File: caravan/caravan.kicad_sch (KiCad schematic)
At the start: 50 parts

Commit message: Updated caravan
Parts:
- added D?: Diode, Diode_THT:D_DO-41_SOD81_P10.16mm_Horizontal, symbol Diode:1N4007
- added K?: Relay_Automotive_SPDT, symbol microfarad-de:Relay_Automotive_SPDT
- CB?: value (none) -> FI-Schalter
- CB? (x2): value (none) -> LS-Schalter
- D?: value (none) -> Diode; footprint (none) -> Diode_THT:D_DO-41_SOD81_P10.16mm_Horizontal
- F? (x4): value (none) -> 10A
- F?: value (none) -> 100A MEGA
- F?: value (none) -> 2A
- F?: value (none) -> 1A
- F? (x3): value (none) -> 15A
- F? (x3): value (none) -> 5A
- F? (x2): value (none) -> 25A Maxi
- F? (x4): value (none) -> 30A MIDI
- K?: value (none) -> 40A
- P?: value (none) -> Landstrom
- Q?: value (none) -> BC337; footprint (none) -> Package_TO_SOT_THT:TO-92_Inline
- R: value (none) -> 100KΩ
- R?, SW? (x3): value (none) -> (none)
- SC?: value (none) -> Solarpanele
- SW?: value (none) -> Hauptschalter
- TH? (x3): value (none) -> Temp. Sensor
- U?: value (none) -> 12V-24V-Wandler
- U?: value (none) -> Victron SmartShunt 500A
- U?: value (none) -> Anhängerstecker
- U?: value (none) -> BMS 100A
- U? (x4): value (none) -> LiFePo4
- U?: value (none) -> Dometic 10 Kühlschrank
- U?: value (none) -> Victron SmartSolar
- U?: value (none) -> Votronic VCC 1212-20 C
- U?: value (none) -> AL-KO ATC
- U?: value (none) -> Ideale Diode 15A
- U?: value (none) -> Victron Blue Smart IP22
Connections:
- net Earth: now also D?.2 (A), F?.1, K?.86, D?.2 (A), K?.30, K?.86, K?.87a
- new net: CB?.1, U?.~ (PE), U?.~ (PE)
- new net: CB?.3, U?.~ (PE), U?.~ (PE)
- new net: D?.1 (K), K?.85, K?.87, U?.~ (PV-)
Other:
- note added: "Kühlschrank-Vorrangschaltung: Leitet überschüssige Solarenergie in den Absorber-Kühlschrank um."
- note added: "MPPT 100/20 Solarladeregler"
- note added: "SunPower 2x120 Watt"

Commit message: Updated caravan and water-sensor
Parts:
- removed D? (x2): Diode, Diode_THT:D_DO-41_SOD81_P10.16mm_Horizontal, symbol Diode:1N4007
- added D? (x2): 1N4007, Diode_THT:D_DO-41_SOD81_P10.16mm_Horizontal, symbol Diode:1N4007
- added F? (x3): 1A, symbol Device:Fuse
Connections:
- net 25mm2 is gone; now on net Earth: F?.1, F?.2, SW?.1 (A), TH?.1, U?.~ (-), U?.~ (-), U?.~ (TS), U?.~ (VBatt+)
- net Earth: now also F?.2, F?.2, F?.2, F?.2, F?.2, K?.85, K?.87, F?.2, F?.2; no longer SW?.2 (B)
- new net: CB?.1, U?.~ (PE), U?.~ (PE)
- new net: CB?.3, U?.~ (PE), U?.~ (PE)
- new net: D?.1 (K), D?.1 (K), U?.~ (PE)
- new net: F?.1, U?.~ (PV-)
- new net: F?.1, SW?.2 (B)
- new net: D?.2 (A), F?.1
- new net: D?.2 (A), F?.2
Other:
- note added: "12V- Verteiler unten"
- note added: "12V-Verteiler oben"
- note added: "4x Wago-Klemmen"
- note added: "ATC+"
- note added: "D+"
- note added: "Dauerplus"
- note added: "Kühlschrank/Reserve"
- note added: "Notizen zur 12V-Verteilung: Die Beleuchtung und Wasserpumpe werden von verschiedenen Stromkreisen gespeist. Dies verhindert das Flackern der Lichter beim Start der Wasserpumpe."
- note removed: "12V-Verteiler"
- note removed: "3x Wago-Klemmen"

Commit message: Updated caravan schematic: Rewire solar controller and booster
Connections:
- new net: CB?.1, U?.~ (PE), U?.~ (PE)
- new net: CB?.3, U?.~ (PE), U?.~ (PE)

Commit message: Caravan schematic: Annotations
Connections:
- new net: CB?.1, U?.~ (PE), U?.~ (PE)
- new net: CB?.3, U?.~ (PE), U?.~ (PE)
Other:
- note added: "24 V"
- note added: "ACHTUNG: Um Störungen zu vermeiden, die Truma-Combi vor dem Betätigen des Batterie-Hauptschalters vollständig auschalten!"
- note added: "Booster"
- note added: "Ladewandler (Booster) (Nr. 3321)"
- note added: "Tank- Heizung"
- note removed: "Ladewandler (Nr. 3321)"
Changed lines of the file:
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@@
+    (effects (font (size 1.27 1.27)) (justify left bottom))
+  )
+  (text "24 V" (at 137.795 168.275 0)
     (effects (font (size 1.27 1.27)) (justify left bottom))
   )
@@
     (effects (font (size 1.27 1.27)) (justify left bottom))
   )
-  (text "Ladewandler (Nr. 3321)" (at 112.395 85.09 0)
+  (text "Ladewandler (Booster) \n(Nr. 3321)" (at 112.395 86.36 0)
     (effects (font (size 1.27 1.27)) (justify left bottom))
   )
@@
     (effects (font (size 1.27 1.27)) (justify left bottom))
   )
+  (text "Tank-\nHeizung" (at 137.795 173.355 0)
+    (effects (font (size 1.27 1.27)) (justify left bottom))
+  )
   (text "Batterie-Verteiler" (at 89.535 239.395 0)
     (effects (font (size 1.27 1.27)) (justify left bottom))
@@
   )
   (text "Kühlschrank/Reserve" (at 108.585 209.55 90)
+    (effects (font (size 1.27 1.27)) (justify left bottom))
+  )
+  (text "Booster" (at 137.795 176.53 0)
     (effects (font (size 1.27 1.27)) (justify left bottom))
   )
@@
     (effects (font (size 1.27 1.27)) (justify left bottom))
   )
-  (text "MPPT 100/20\nSolarladeregler" (at 219.71 86.995 0)
+  (text "MPPT 100/20\nSolarladeregler" (at 216.535 86.995 0)
     (effects (font (size 1.27 1.27)) (justify left bottom))
   )
@@
     (effects (font (size 1.27 1.27)) (justify left bottom))
   )
+  (text "ACHTUNG:\nUm Störungen zu vermeiden,\ndie Truma-Combi vor dem Betätigen \ndes Batterie-Hauptschalters \nvollständig auschalten!"
+    (at 219.71 50.8 0)
+    (effects (font (size 1.778 1.778) (thickness 0.254) bold) (justify left bottom))
+  )
   (text "Kleiderschrank" (at 77.47 39.37 0)

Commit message: Updated caravan
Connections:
- new net: CB?.1, U?.~ (PE), U?.~ (PE)
- new net: CB?.3, U?.~ (PE), U?.~ (PE)
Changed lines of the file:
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@@
   (title_block
     (title "Autark-Schaltplan")
-    (date "2023-10-27")
+    (date "2023-12-21")
     (comment 1 "Fendt Bianco Activ 390 FHS Autark-Schaltplan")
   )
@@
     (stroke (width 0) (type default) (color 0 0 0 0))
   )
-  (wire (pts (xy 226.06 184.785) (xy 226.06 185.42))
+  (wire (pts (xy 226.06 152.4) (xy 226.06 185.42))
     (stroke (width 0) (type default) (color 0 0 0 0))
   )
@@
     (stroke (width 0) (type default) (color 0 0 0 0))
   )
+  (wire (pts (xy 217.805 99.06) (xy 217.805 152.4))
+    (stroke (width 0) (type default) (color 0 0 0 0))
+  )
   (wire (pts (xy 123.825 193.675) (xy 164.465 193.675))
     (stroke (width 0) (type default) (color 0 0 0 0))
@@
     (stroke (width 0) (type default) (color 0 0 0 0))
   )
-  (wire (pts (xy 218.44 185.42) (xy 219.71 182.245))
+  (wire (pts (xy 218.44 156.21) (xy 218.44 185.42))
     (stroke (width 0) (type default) (color 0 0 0 0))
   )
@@
     (stroke (width 0) (type default) (color 0 0 0 0))
   )
-  (wire (pts (xy 219.71 156.21) (xy 219.71 182.245))
-    (stroke (width 0) (type default) (color 0 0 0 0))
-  )
   (wire (pts (xy 355.6 116.205) (xy 355.6 130.175))
     (stroke (width 0) (type default) (color 0 0 0 0))
@@
     (stroke (width 0) (type default) (color 0 0 0 0))
   )
-  (wire (pts (xy 217.805 182.245) (xy 218.44 185.42))
-    (stroke (width 0) (type default) (color 0 0 0 0))
-  )
   (wire (pts (xy 223.52 102.87) (xy 223.52 99.06))
     (stroke (width 0) (type default) (color 0 0 0 0))
@@
     (stroke (width 0) (type default) (color 0 0 0 0))
   )
+  (wire (pts (xy 217.805 152.4) (xy 226.06 152.4))
+    (stroke (width 0) (type default) (color 0 0 0 0))
+  )
   (wire (pts (xy 374.015 109.22) (xy 371.475 109.22))
     (stroke (width 0) (type default) (color 0 0 0 0))
@@
     (stroke (width 0) (type default) (color 0 0 0 0))
   )
-  (wire (pts (xy 217.805 99.06) (xy 217.805 182.245))
-    (stroke (width 0) (type default) (color 0 0 0 0))
-  )
   (wire (pts (xy 140.97 236.855) (xy 135.89 236.855))
     (stroke (width 0) (type default) (color 0 0 0 0))
@@
     (stroke (width 0) (type default) (color 0 0 0 0))
   )
-  (wire (pts (xy 219.71 156.21) (xy 290.195 156.21))
+  (wire (pts (xy 218.44 156.21) (xy 290.195 156.21))
     (stroke (width 0) (type default) (color 0 0 0 0))
   )
@@
     (effects (font (size 1.27 1.27)) (justify left bottom))
   )
-  (text "12V-Verteiler oben" (at 219.71 182.245 90)
+  (text "12V-Verteiler oben" (at 218.44 182.245 90)
     (effects (font (size 1.27 1.27)) (justify left bottom))
   )
@@
     (effects (font (size 1.27 1.27)) (justify left bottom))
   )
-  (text "Solarladeregler" (at 217.805 182.245 90)
-    (effects (font (size 1.27 1.27)) (justify left bottom))
-  )
+  (text "Solarladeregler" (at 226.06 182.245 90)
+    (effects (font (size 1.27 1.27)) (justify left bottom))
+  )

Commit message: Updated water-alarm
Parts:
- F?: value 15A -> 5A
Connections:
- new net: CB?.1, U?.~ (PE), U?.~ (PE)
- new net: CB?.3, U?.~ (PE), U?.~ (PE)
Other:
- note added: "ACHTUNG: Um Störungen zu vermeiden, schalten Sie die Truma-Combi vollständig aus, bevor Sie den Batterie-Hauptschalter betätigen!"
- note added: "Hinweis zur 12V-Verteilung: Die Beleuchtung und die Wasserpumpe werden von verschiedenen Stromkreisen versorgt. Dies verhindert, dass die Lichter beim Start der Wasserpumpe flackern."
- note added: "Hinweise zum Votronic Ladewandler: Das Relais unterbindet den Rückladezweig und verhindert damit das Einschalten des ATC ohne Zugfahrzeug. Der Transistor aktiviert den Ladevorgang nur, wenn ATC-Schaltplus und Zugfahrzeug-D+ beide aktiv sind. Dadurch wird der Ladevorgang unterbrochen, wenn der Motor aus ist oder die ATC-Bremse aktiv ist. Die ideale Diode ermöglicht das gleichzeitige Nutzen der Sch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"
- note added: "Maxxfan Lüfter"
- note removed: "ACHTUNG: Um Störungen zu vermeiden, die Truma-Combi vor dem Betätigen des Batterie-Hauptschalters vollständig auschalten!"
- note removed: "Notizen zum Votronic Ladewandler: Das Relais unterbindet den Rückladezweig und verhindert damit das Einschalten vom ATC ohne Zugfahrzeug. Der Transistor aktiviert den Ladevorgang nur wenn ATC-Schaltplus UND Zugfahrzeug-D+ beide aktiv sind. Damit wird der Ladevorgang unterbrochen, wenn der Motor aus oder die ATC-Bremse aktiv ist. Die Ideale Diode ermöglicht das gleichzeitige Nutzen der Shaltplus- 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"
- note removed: "Notizen zur 12V-Verteilung: Die Beleuchtung und Wasserpumpe werden von verschiedenen Stromkreisen gespeist. Dies verhindert das Flackern der Lichter beim Start der Wasserpumpe."
- note removed: "Reserve"
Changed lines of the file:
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@@
   (title_block
     (title "Autark-Schaltplan")
-    (date "2023-12-21")
+    (date "2024-06-18")
     (comment 1 "Fendt Bianco Activ 390 FHS Autark-Schaltplan")
   )
@@
     (effects (font (size 1.27 1.27)) (justify left bottom))
   )
-  (text "Reserve" (at 374.65 102.235 0)
+  (text "Maxxfan Lüfter" (at 374.65 102.235 0)
     (effects (font (size 1.27 1.27)) (justify left bottom))
   )
@@
     (effects (font (size 1.27 1.27)) (justify left bottom))
   )
-  (text "Notizen zur 12V-Verteilung:\nDie Beleuchtung und Wasserpumpe werden von \nverschiedenen Stromkreisen gespeist.\nDies verhindert das Flackern der Lichter beim \nStart der Wasserpumpe."
-    (at 160.02 58.42 0)
+  (text "Hinweis zur 12V-Verteilung:\n\nDie Beleuchtung und die Wasserpumpe werden \nvon verschiedenen Stromkreisen versorgt. \nDies verhindert, dass die Lichter beim Start \nder Wasserpumpe flackern."
+    (at 162.56 57.15 0)
     (effects (font (size 1.27 1.27)) (justify left bottom))
   )
@@
     (effects (font (size 1.27 1.27)) (justify left bottom))
   )
-  (text "Notizen zum Votronic Ladewandler:\nDas Relais unterbindet den Rückladezweig und verhindert damit das\nEinschalten vom ATC ohne Zugfahrzeug.\nDer Transistor aktiviert den Ladevorgang nur wenn ATC-Schaltplus UND \nZugfahrzeug-D+ beide aktiv sind. Damit wird der Ladevorgang unterbrochen,\nwenn der Motor aus oder die ATC-Bremse aktiv ist. \nDie Ideale Diode ermöglicht das gleichzeitige Nutzen der Shaltplus- und \nDauerplus-Leitungen zum Laden der Batterie. Dies ermöglicht die\noptimale Nutzung des Leitungsquerschnitts.\nDer Ladewandler kann mittels eines Schalters deaktiviert werden."
-    (at 77.47 68.58 0)
+  (text "Hinweise zum Votronic Ladewandler:\n\nDas Relais unterbindet den Rückladezweig und verhindert damit das \nEinschalten des ATC ohne Zugfahrzeug. \n\nDer Transistor aktiviert den Ladevorgang nur, wenn ATC-Schaltplus und \nZugfahrzeug-D+ beide aktiv sind. Dadurch wird der Ladevorgang unterbrochen, \nwenn der Motor aus ist oder die ATC-Bremse aktiv ist. \n\nDie ideale Diode ermöglicht das gleichzeitige Nutzen der Schaltplus- und \nDauerplus-Leitungen zum Laden der Batterie, wodurch die optimale Nutzung \ndes Leitungsquerschnitts ermöglicht wird. Der Ladewandler kann mittels \neines Schalters deaktiviert werden."
+    (at 77.47 71.755 0)
     (effects (font (size 1.27 1.27)) (justify left bottom))
   )
@@
     (effects (font (size 1.27 1.27)) (justify left bottom))
   )
-  (text "ACHTUNG:\nUm Störungen zu vermeiden,\ndie Truma-Combi vor dem Betätigen \ndes Batterie-Hauptschalters \nvollständig auschalten!"
-    (at 219.71 50.8 0)
-    (effects (font (size 1.778 1.778) (thickness 0.254) bold) (justify left bottom))
+  (text "ACHTUNG: \n\nUm Störungen zu vermeiden, schalten Sie \ndie Truma-Combi vollständig aus, bevor Sie \nden Batterie-Hauptschalter betätigen!"
+    (at 219.71 54.61 0)
+    (effects (font (size 1.27 1.27)) (justify left bottom))
   )
   (text "Kleiderschrank" (at 77.47 39.37 0)
@@
       (effects (font (size 1.27 1.27)) (justify left) hide)
     )
-    (property "Value" "15A" (id 1) (at 363.855 102.87 90)
+    (property "Value" "5A" (id 1) (at 363.855 102.87 90)
       (effects (font (size 1.27 1.27)) (justify left))
     )
@@
     )
     (path "/00000000-0000-0000-0000-00006175cae2"
-      (reference "F?") (unit 1) (value "15A") (footprint "")
+      (reference "F?") (unit 1) (value "5A") (footprint "")
     )
     (path "/00000000-0000-0000-0000-00006175cfd8"

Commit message: Updated caravan
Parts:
- removed F?: 1A, symbol Device:Fuse
- removed K?: Relay_Automotive_SPDT, symbol microfarad-de:Relay_Automotive_SPDT
- removed U?: Dometic 10 Kühlschrank, symbol caravan-rescue:Dometic_Fridge-microfarad-de
- added D?: LED, symbol Device:LED
- added F?: 15A, symbol Device:Fuse
- added K?: Relais, symbol caravan-rescue:Relay_Automotive_SPST-microfarad-de
- added M? (x2): Lüfter, symbol Motor:Fan
- added R?: 680Ω, symbol Device:R
- added U?: Verzögerung, symbol microfarad-de:555_Delay
- added U?: Isotherm Kühlaggregat, symbol microfarad-de:Isotherm
- added U?: Kühlschrank, symbol microfarad-de:Dometic_Fridge_2
- F? (x2): value 15A -> 20A
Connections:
- net Earth: now also F?.1, U?. (PE), U?. (T); no longer F?.1, K?.86
- net at CB?.1, U?.~ (PE): now also U?. (PE)
- net at CB?.3, U?.~ (PE): now also U?. (PE)
- net at F?.1: now also U?. (PE)
- net at D?.1 (K), D?.1 (K): now also U?. (PE)
- net at K?.85, Q?.1 (C), SW?.1 (A): now also D?.2 (A)
- new net: F?.1, K?.86, U?.~ (OUT-)
- new net: R?.1, U?. (T)
- new net: K?.30, R?.2
- new net: K?.85, U?. (OUT-)
- new net: K?.86, U?. (OUT-)
- new net: U?. (OUT-), U?. (PE) (x2)
- new net: K?.87, U?. (T)
- new net: D?.1 (K), U?. (T)
- new net: D?.2 (A), M?.1 (+), M?.1 (+), U?. (T)
- new net: M?.2 (-), M?.2 (-), U?. (T)
- new net: F?.2, U?. (T)
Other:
- note added: "12V-Stecker"
- note added: "2 Minuten"
- note added: "230V-Stecker"
- note added: "Die 12V-Heizpatrone wurde deaktiviert und durch das Isotherm Kompressor-Kühlaggregat ersetzt."
- note added: "Dometic RML 10.4 Absorberkühlschrank"
- note added: "Draußen"
- note added: "Kühlschrank-Steuerung: Der D+ Signal wird in den folgenden fällen aktiviert: • Ausreichende Batteriespannung • Der Ladewandler (Booster) aktiv ist"
- note added: "Secop BD35 Kompressor"
- note removed: "Kühlschrank-Vorrangschaltung: Leitet überschüssige Solarenergie in den Absorber-Kühlschrank um."

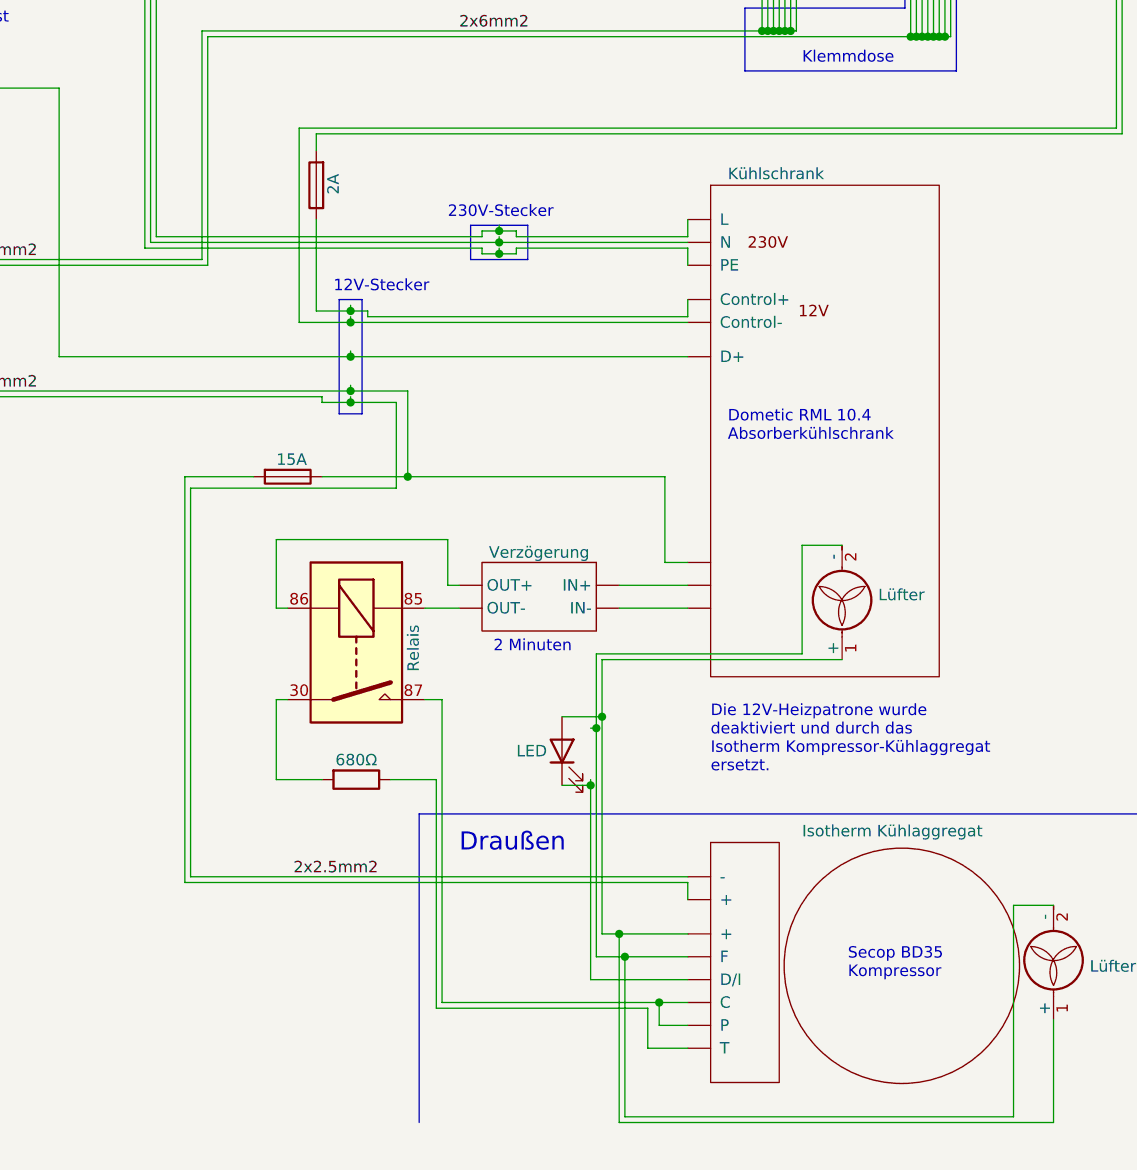
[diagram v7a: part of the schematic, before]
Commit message: Renamed delay-timer to 555-delay Updated caravan
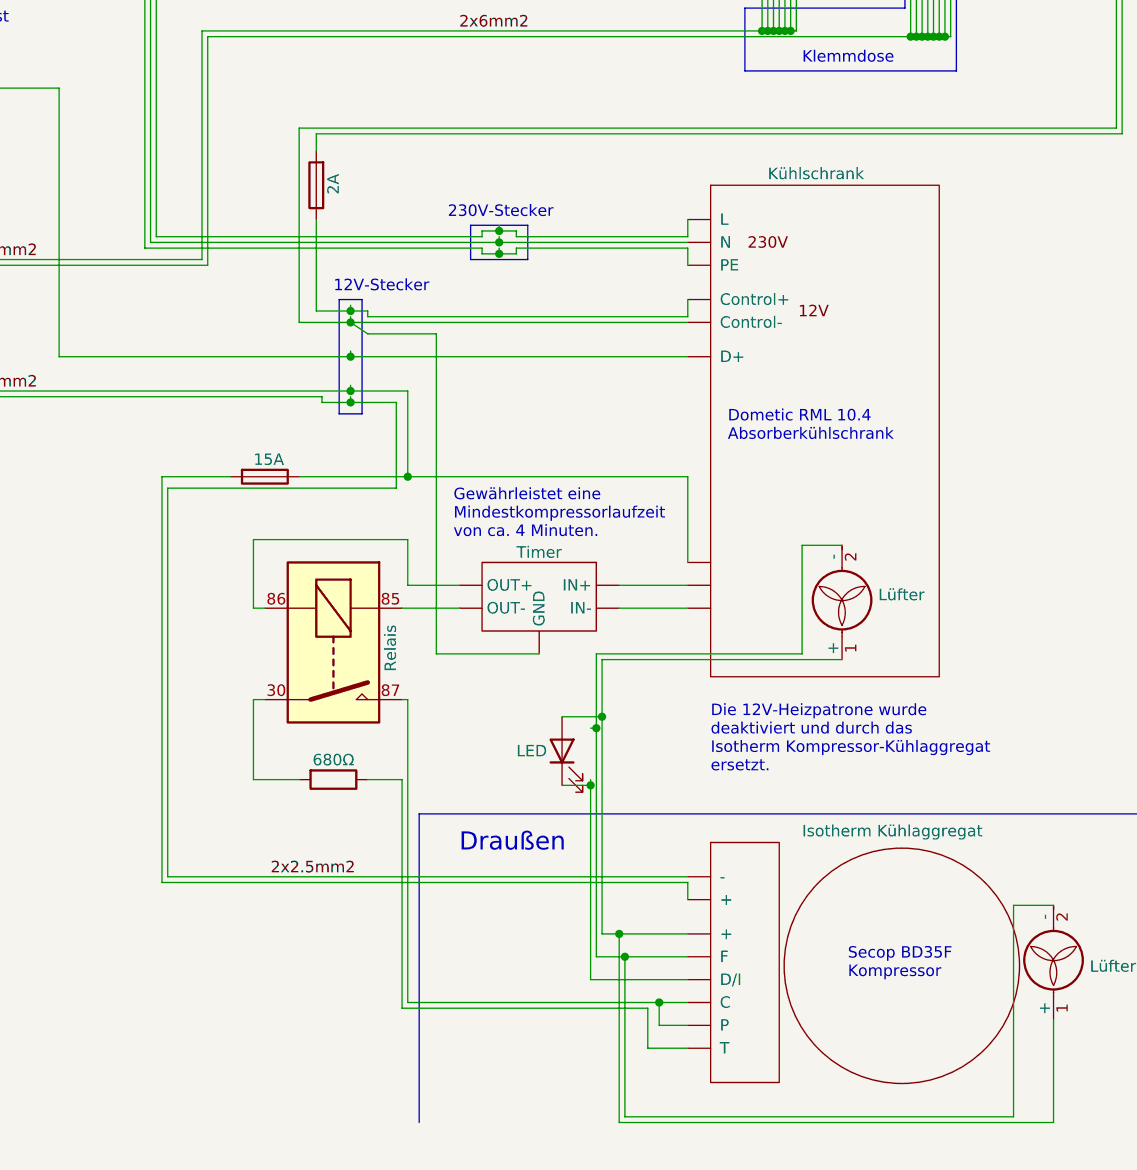
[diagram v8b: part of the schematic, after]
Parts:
- U?: value Verzögerung -> Timer
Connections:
- net Earth: now also U?. (OUT-)
- new net: CB?.1, U?. (PE), U?.~ (PE)
- new net: CB?.3, U?. (PE), U?.~ (PE)
- new net: U?. (OUT-), U?. (PE) (x2)
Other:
- note added: "Gewährleistet eine Mindestkompressorlaufzeit von ca. 4 Minuten."
- note added: "Secop BD35F Kompressor"
- note removed: "2 Minuten"
- note removed: "Secop BD35 Kompressor"
